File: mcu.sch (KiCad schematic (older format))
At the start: 26 parts, among them SW1 PTS645VL39-2, U4 CAT24C32, U5 STM32F765VIT6, X1 ECS-TXO-3225-160-TR

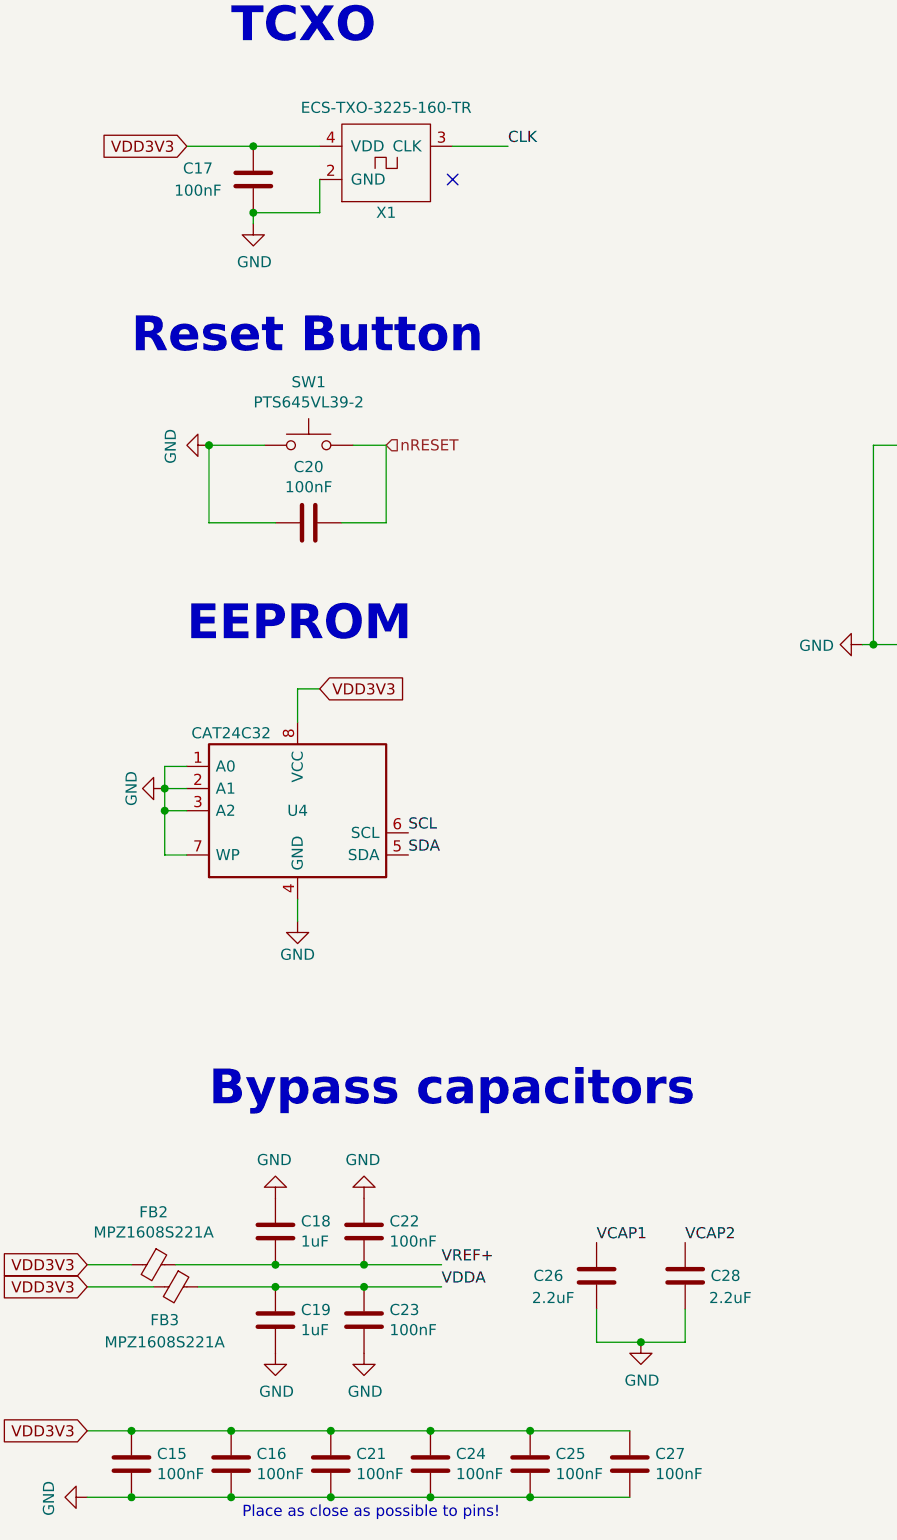
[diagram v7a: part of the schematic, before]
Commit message: Add bypass cap for I2C EEPROMs and redone some copper pour
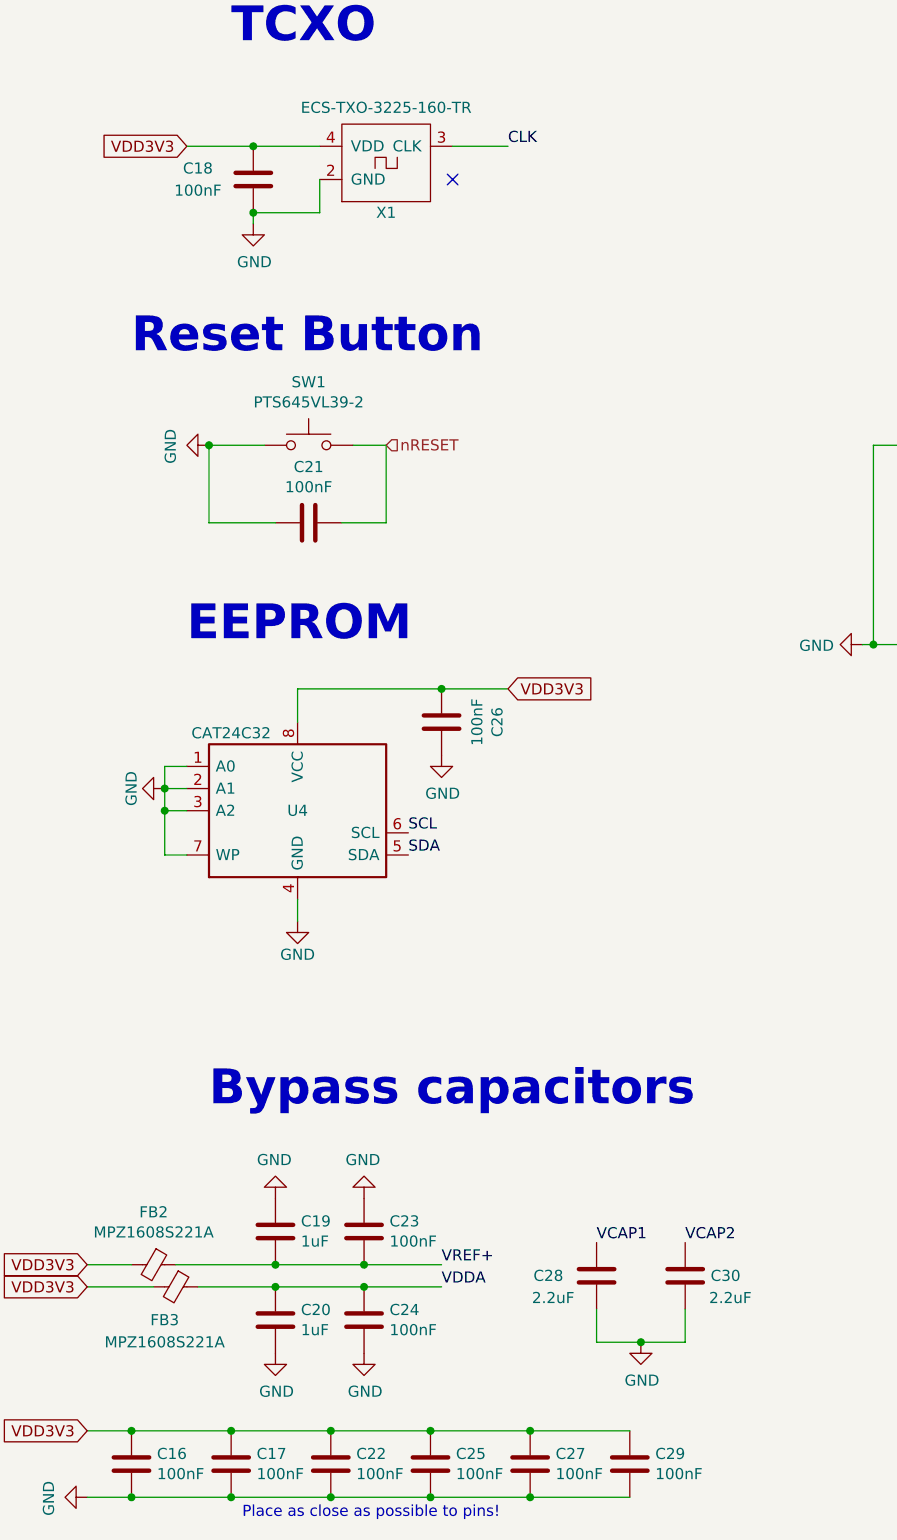
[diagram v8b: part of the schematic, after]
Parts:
- added C26: 100nF, Capacitor_SMD:C_0603_1608Metric, symbol Device:C
- renumbered C15 to C16, C16 to C17, C17 to C18, C18 to C19, C19 to C20, C20 to C21, C21 to C22, C22 to C23, C23 to C24, C24 to C25, C25 to C27, C26 to C28, C27 to C29, C28 to C30
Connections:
- net GND: now also C26.2
- net VDD3V3: now also C26.1
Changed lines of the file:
@@
 VDD3V3
 $Comp
-L Device:C C19
+L Device:C C20
 U 1 1 5AD085F7
 P 1800 6650
-F 0 "C19" H 1915 6696 50  0000 L CNN
+F 0 "C20" H 1915 6696 50  0000 L CNN
 F 1 "1uF" H 1915 6605 50  0000 L CNN
 F 2 "Capacitor_SMD:C_0603_1608Metric" H 1838 6500 50  0001 C CNN
@@
 $EndComp
 $Comp
-L Device:C C23
+L Device:C C24
 U 1 1 5AD086E9
 P 2200 6650
-F 0 "C23" H 2315 6696 50  0000 L CNN
+F 0 "C24" H 2315 6696 50  0000 L CNN
 F 1 "100nF" H 2315 6605 50  0000 L CNN
 F 2 "Capacitor_SMD:C_0603_1608Metric" H 2238 6500 50  0001 C CNN
@@
 VDD3V3
 $Comp
-L Device:C C18
+L Device:C C19
 U 1 1 5AD08A76
 P 1800 6250
-F 0 "C18" H 1915 6296 50  0000 L CNN
+F 0 "C19" H 1915 6296 50  0000 L CNN
 F 1 "1uF" H 1915 6205 50  0000 L CNN
 F 2 "Capacitor_SMD:C_0603_1608Metric" H 1838 6100 50  0001 C CNN
@@
 $EndComp
 $Comp
-L Device:C C22
+L Device:C C23
 U 1 1 5AD08A7D
 P 2200 6250
-F 0 "C22" H 2315 6296 50  0000 L CNN
+F 0 "C23" H 2315 6296 50  0000 L CNN
 F 1 "100nF" H 2315 6205 50  0000 L CNN
 F 2 "Capacitor_SMD:C_0603_1608Metric" H 2238 6100 50  0001 C CNN
@@
 VDD3V3
 $Comp
-L Device:C C15
+L Device:C C16
 U 1 1 5AD0945E
 P 1150 7300
-F 0 "C15" H 1265 7346 50  0000 L CNN
+F 0 "C16" H 1265 7346 50  0000 L CNN
 F 1 "100nF" H 1265 7255 50  0000 L CNN
 F 2 "Capacitor_SMD:C_0603_1608Metric" H 1188 7150 50  0001 C CNN
@@
 $EndComp
 $Comp
-L Device:C C16
+L Device:C C17
 U 1 1 5AD09C8C
 P 1600 7300
-F 0 "C16" H 1715 7346 50  0000 L CNN
+F 0 "C17" H 1715 7346 50  0000 L CNN
 F 1 "100nF" H 1715 7255 50  0000 L CNN
 F 2 "Capacitor_SMD:C_0603_1608Metric" H 1638 7150 50  0001 C CNN
@@
 $EndComp
 $Comp
-L Device:C C21
+L Device:C C22
 U 1 1 5AD09D94
 P 2050 7300
-F 0 "C21" H 2165 7346 50  0000 L CNN
+F 0 "C22" H 2165 7346 50  0000 L CNN
 F 1 "100nF" H 2165 7255 50  0000 L CNN
 F 2 "Capacitor_SMD:C_0603_1608Metric" H 2088 7150 50  0001 C CNN
@@
 $EndComp
 $Comp
-L Device:C C24
+L Device:C C25
 U 1 1 5AD09D9B
 P 2500 7300
-F 0 "C24" H 2615 7346 50  0000 L CNN
+F 0 "C25" H 2615 7346 50  0000 L CNN
 F 1 "100nF" H 2615 7255 50  0000 L CNN
 F 2 "Capacitor_SMD:C_0603_1608Metric" H 2538 7150 50  0001 C CNN
@@
 $EndComp
 $Comp
-L Device:C C25
+L Device:C C27
 U 1 1 5AD09E94
 P 2950 7300
-F 0 "C25" H 3065 7346 50  0000 L CNN
+F 0 "C27" H 3065 7346 50  0000 L CNN
 F 1 "100nF" H 3065 7255 50  0000 L CNN
 F 2 "Capacitor_SMD:C_0603_1608Metric" H 2988 7150 50  0001 C CNN
@@
 VDD3V3
 $Comp
-L Device:C C26
+L Device:C C28
 U 1 1 5AD0FCE6
 P 3250 6450
-F 0 "C26" H 3400 6450 50  0000 L CNN
+F 0 "C28" H 3400 6450 50  0000 L CNN
 F 1 "2.2uF" H 3350 6550 50  0000 L CNN
 F 2 "Capacitor_SMD:C_0603_1608Metric" H 3288 6300 50  0001 C CNN
@@
 $EndComp
 $Comp
-L Device:C C28
+L Device:C C30
 U 1 1 5AD117D1
 P 3650 6450
-F 0 "C28" H 3400 6450 50  0000 L CNN
+F 0 "C30" H 3400 6450 50  0000 L CNN
 F 1 "2.2uF" H 3350 6550 50  0000 L CNN
 F 2 "Capacitor_SMD:C_0603_1608Metric" H 3688 6300 50  0001 C CNN
@@
 $EndComp
 $Comp
-L power:GND #PWR038
+L power:GND #PWR039
 U 1 1 5AF579EA
 P 2200 6800
-F 0 "#PWR038" H 2200 6550 50  0001 C CNN
+F 0 "#PWR039" H 2200 6550 50  0001 C CNN
 F 1 "GND" H 2205 6627 50  0000 C CNN
 F 2 "" H 2200 6800 50  0001 C CNN
@@
 $EndComp
 $Comp
-L power:GND #PWR035
+L power:GND #PWR036
 U 1 1 5AF580A3
 P 1800 6800
-F 0 "#PWR035" H 1800 6550 50  0001 C CNN
+F 0 "#PWR036" H 1800 6550 50  0001 C CNN
 F 1 "GND" H 1805 6627 50  0000 C CNN
 F 2 "" H 1800 6800 50  0001 C CNN
@@
 $EndComp
 $Comp
-L power:GND #PWR034
+L power:GND #PWR035
 U 1 1 5AF58792
 P 1800 6100
-F 0 "#PWR034" H 1800 5850 50  0001 C CNN
+F 0 "#PWR035" H 1800 5850 50  0001 C CNN
 F 1 "GND" H 1805 5927 50  0000 C CNN
 F 2 "" H 1800 6100 50  0001 C CNN
@@
 $EndComp
 $Comp
-L power:GND #PWR037
+L power:GND #PWR038
 U 1 1 5AF59C69
 P 2200 6100
-F 0 "#PWR037" H 2200 5850 50  0001 C CNN
+F 0 "#PWR038" H 2200 5850 50  0001 C CNN
 F 1 "GND" H 2205 5927 50  0000 C CNN
 F 2 "" H 2200 6100 50  0001 C CNN
@@
 $EndComp
 $Comp
-L power:GND #PWR040
+L power:GND #PWR042
 U 1 1 5AF5BF00
 P 4450 3600
-F 0 "#PWR040" H 4450 3350 50  0001 C CNN
+F 0 "#PWR042" H 4450 3350 50  0001 C CNN
 F 1 "GND" V 4455 3472 50  0000 R CNN
 F 2 "" H 4450 3600 50  0001 C CNN
@@
 $EndComp
 $Comp
-L power:GND #PWR042
+L power:GND #PWR044
 U 1 1 5AF5CFF3
 P 5650 850
-F 0 "#PWR042" H 5650 600 50  0001 C CNN
+F 0 "#PWR044" H 5650 600 50  0001 C CNN
 F 1 "GND" H 5655 677 50  0000 C CNN
 F 2 "" H 5650 850 50  0001 C CNN
@@
 $EndComp
 $Comp
-L power:GND #PWR044
+L power:GND #PWR046
 U 1 1 5AF5E7FC
 P 9300 1900
-F 0 "#PWR044" H 9300 1650 50  0001 C CNN
+F 0 "#PWR046" H 9300 1650 50  0001 C CNN
 F 1 "GND" H 9300 1750 50  0000 C CNN
 F 2 "" H 9300 1900 50  0001 C CNN
@@
 $EndComp
 $Comp
-L power:GND #PWR043
+L power:GND #PWR045
 U 1 1 5AF5F2E4
 P 7850 5200
-F 0 "#PWR043" H 7850 4950 50  0001 C CNN
+F 0 "#PWR045" H 7850 4950 50  0001 C CNN
 F 1 "GND" H 7855 5027 50  0000 C CNN
 F 2 "" H 7850 5200 50  0001 C CNN
@@
 $EndComp
 $Comp
-L power:GND #PWR032
+L power:GND #PWR033
 U 1 1 5AF616AA
 P 1500 2700
-F 0 "#PWR032" H 1500 2450 50  0001 C CNN
+F 0 "#PWR033" H 1500 2450 50  0001 C CNN
 F 1 "GND" H 1505 2527 50  0000 C CNN
 F 2 "" H 1500 2700 50  0001 C CNN
@@
 	1500 2700 1750 2700
 $Comp
-L Device:C C20
+L Device:C C21
 U 1 1 5AF62329
 P 1950 3050
-F 0 "C20" V 2202 3050 50  0000 C CNN
+F 0 "C21" V 2202 3050 50  0000 C CNN
 F 1 "100nF" V 2111 3050 50  0000 C CNN
 F 2 "Capacitor_SMD:C_0603_1608Metric" H 1988 2900 50  0001 C CNN
@@
 	1500 3050 1800 3050
 $Comp
-L power:GND #PWR045
+L power:GND #PWR047
 U 1 1 5AF66D47
 P 10450 5700
-F 0 "#PWR045" H 10450 5450 50  0001 C CNN
+F 0 "#PWR047" H 10450 5450 50  0001 C CNN
 F 1 "GND" H 10455 5527 50  0000 C CNN
 F 2 "" H 10450 5700 50  0001 C CNN
@@
 	2300 3050 2300 2700
 $Comp
-L power:GND #PWR030
+L power:GND #PWR031
 U 1 1 5AFDE2A1
 P 950 7450
-F 0 "#PWR030" H 950 7200 50  0001 C CNN
+F 0 "#PWR031" H 950 7200 50  0001 C CNN
 F 1 "GND" H 955 7277 50  0000 C CNN
 F 2 "" H 950 7450 50  0001 C CNN
@@
 $EndComp
 $Comp
-L power:GND #PWR033
+L power:GND #PWR034
 U 1 1 5BC52E02
 P 1700 1700
-F 0 "#PWR033" H 1700 1450 50  0001 C CNN
+F 0 "#PWR034" H 1700 1450 50  0001 C CNN
 F 1 "GND" H 1705 1527 50  0000 C CNN
 F 2 "" H 1700 1700 50  0001 C CNN
@@
 $EndComp
 $Comp
-L Device:C C17
+L Device:C C18
 U 1 1 5BC55501
 P 1700 1500
-F 0 "C17" H 1450 1550 50  0000 C CNN
+F 0 "C18" H 1450 1550 50  0000 C CNN
 F 1 "100nF" H 1450 1450 50  0000 C CNN
 F 2 "Capacitor_SMD:C_0603_1608Metric" H 1738 1350 50  0001 C CNN
@@
 AR Path="/5BC1FDFA" Ref="#PWR?"  Part="1"
 AR Path="/5BC4AC32/5BC1FDFA" Ref="#PWR?"  Part="1"
-AR Path="/5BC1C8A4/5BC1FDFA" Ref="#PWR031"  Part="1"
-F 0 "#PWR031" H 1300 4000 50  0001 C CNN
+AR Path="/5BC1C8A4/5BC1FDFA" Ref="#PWR032"  Part="1"
+F 0 "#PWR032" H 1300 4000 50  0001 C CNN
 F 1 "GND" H 1300 4100 50  0000 C CNN
 F 2 "" H 1300 4250 50  0000 C CNN
@@
 P 1900 4850
 AR Path="/5BC4AC32/5BC1FE00" Ref="#PWR?"  Part="1"
-AR Path="/5BC1C8A4/5BC1FE00" Ref="#PWR036"  Part="1"
-F 0 "#PWR036" H 1900 4600 50  0001 C CNN
+AR Path="/5BC1C8A4/5BC1FE00" Ref="#PWR037"  Part="1"
+F 0 "#PWR037" H 1900 4600 50  0001 C CNN
 F 1 "GND" H 1900 4700 50  0000 C CNN
 F 2 "" H 1900 4850 50  0000 C CNN
@@
 Wire Wire Line
 	1300 4250 1400 4250
-Text GLabel 2000 3800 2    50   Input ~ 0
+Text GLabel 2850 3800 2    50   Input ~ 0
 VDD3V3
 Wire Wire Line
 	1900 3950 1900 3800
-Wire Wire Line
-	1900 3800 2000 3800
 Text GLabel 5150 2300 0    50   Input ~ 0
 VDD3V3
 $Comp
-L Device:C C27
+L Device:C C29
 U 1 1 5BC224AB
 P 3400 7300
-F 0 "C27" H 3515 7346 50  0000 L CNN
+F 0 "C29" H 3515 7346 50  0000 L CNN
 F 1 "100nF" H 3515 7255 50  0000 L CNN
 F 2 "Capacitor_SMD:C_0603_1608Metric" H 3438 7150 50  0001 C CNN
@@
 VCAP2
 $Comp
-L power:GND #PWR039
+L power:GND #PWR041
 U 1 1 5BCFC2D0
 P 3450 6750
-F 0 "#PWR039" H 3450 6500 50  0001 C CNN
+F 0 "#PWR041" H 3450 6500 50  0001 C CNN
 F 1 "GND" H 3455 6577 50  0000 C CNN
 F 2 "" H 3450 6750 50  0001 C CNN
@@
 $EndComp
 $Comp
-L power:GND #PWR041
+L power:GND #PWR043
 U 1 1 5BCEB458
 P 5550 6700
-F 0 "#PWR041" H 5550 6450 50  0001 C CNN
+F 0 "#PWR043" H 5550 6450 50  0001 C CNN
 F 1 "GND" H 5555 6527 50  0000 C CNN
 F 2 "" H 5550 6700 50  0001 C CNN
@@
 $EndComp
 NoConn ~ 2600 1500
+$Comp
+L Device:C C26
+U 1 1 5BD1182C
+P 2550 3950
+F 0 "C26" V 2802 3950 50  0000 C CNN
+F 1 "100nF" V 2711 3950 50  0000 C CNN
+F 2 "Capacitor_SMD:C_0603_1608Metric" H 2588 3800 50  0001 C CNN
+F 3 "~" H 2550 3950 50  0001 C CNN
+	1    2550 3950
+	1    0    0    -1
+$EndComp
+$Comp
+L power:GND #PWR040
+U 1 1 5BD14C12
+P 2550 4100
+F 0 "#PWR040" H 2550 3850 50  0001 C CNN
+F 1 "GND" H 2555 3927 50  0000 C CNN
+F 2 "" H 2550 4100 50  0001 C CNN
+F 3 "" H 2550 4100 50  0001 C CNN
+	1    2550 4100
+	1    0    0    -1
+$EndComp
+Wire Wire Line
+	2850 3800 2550 3800
+Wire Wire Line
+	1900 3800 2550 3800
+Connection ~ 2550 3800
 $EndSCHEMATC
